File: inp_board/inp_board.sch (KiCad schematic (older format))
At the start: 2 parts

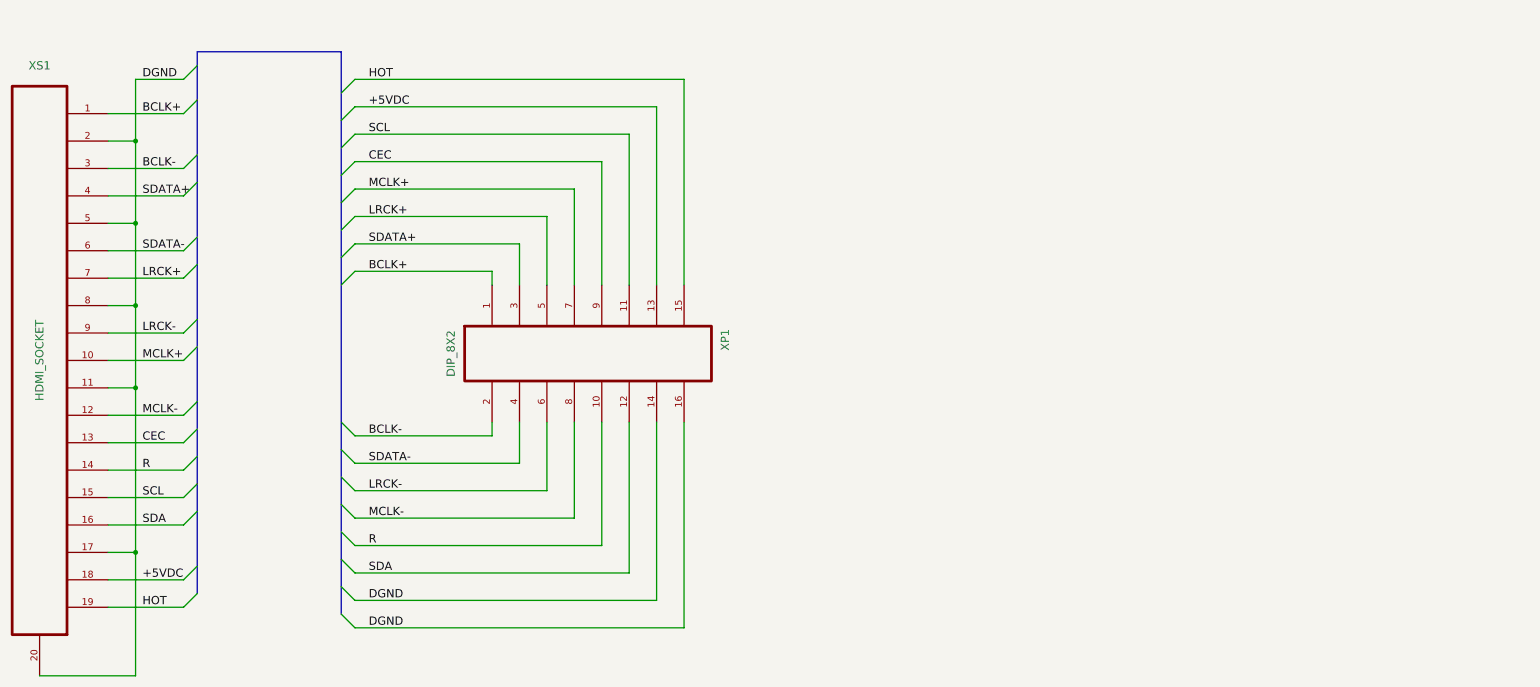
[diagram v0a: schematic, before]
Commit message: spdif part added
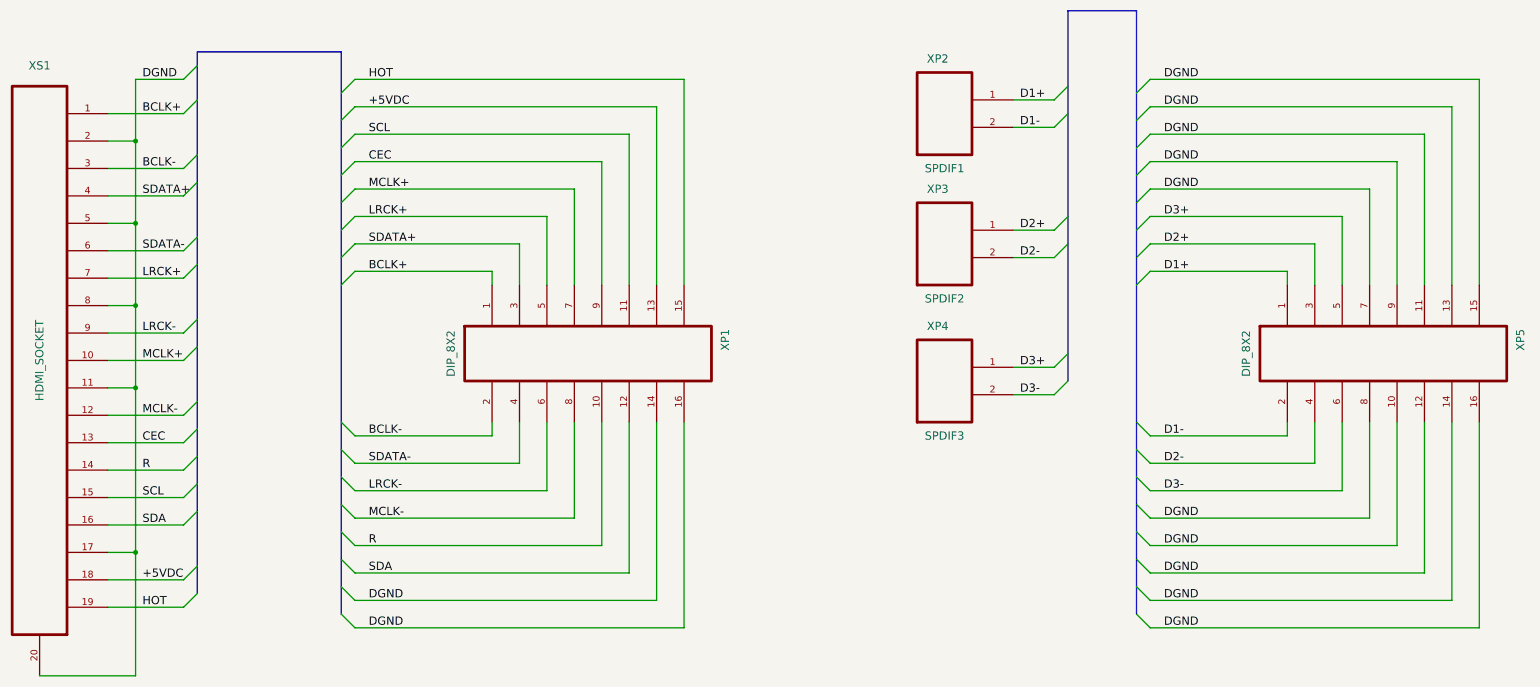
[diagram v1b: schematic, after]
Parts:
- added XP2: SPDIF1, ~, symbol RCA_CONN
- added XP3: SPDIF2, ~, symbol RCA_CONN
- added XP4: SPDIF3, ~, symbol RCA_CONN
- added XP5: DIP_8X2, symbol DIP_8X2
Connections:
- net DGND: now also XP5.10, XP5.11, XP5.12, XP5.13, XP5.14, XP5.15, XP5.16, XP5.7, XP5.8, XP5.9
- new net D1+: XP2.1, XP5.1
- new net D1-: XP2.2, XP5.2
- new net D2+: XP3.1, XP5.3
- new net D2-: XP3.2, XP5.4
- new net D3+: XP4.1, XP5.5
- new net D3-: XP4.2, XP5.6
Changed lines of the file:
@@
 LIBS:valves
 LIBS:gost
-LIBS:InputASRC-cache
+LIBS:inp_board-cache
 EELAYER 27 0
 EELAYER END
-$Descr A4 11693 8268
+$Descr A3 16535 11693
 encoding utf-8
 Sheet 1 1
 Title "noname.sch"
-Date "10 aug 2013"
+Date "12 aug 2013"
 Rev ""
 Comp ""
@@
 Text Label 4800 1600 0    60   ~ 0
 HOT
+$Comp
+L RCA_CONN XP2
+U 1 1 5208E51C
+P 9000 1850
+F 0 "XP2" H 8950 2250 60  0000 C CNN
+F 1 "SPDIF1" H 9000 1450 60  0000 C CNN
+F 2 "~" H 9200 1850 60  0000 C CNN
+F 3 "~" H 9200 1850 60  0000 C CNN
+	1    9000 1850
+	1    0    0    -1
+$EndComp
+$Comp
+L RCA_CONN XP3
+U 1 1 5208E52B
+P 9000 2800
+F 0 "XP3" H 8950 3200 60  0000 C CNN
+F 1 "SPDIF2" H 9000 2400 60  0000 C CNN
+F 2 "~" H 9200 2800 60  0000 C CNN
+F 3 "~" H 9200 2800 60  0000 C CNN
+	1    9000 2800
+	1    0    0    -1
+$EndComp
+$Comp
+L RCA_CONN XP4
+U 1 1 5208E53A
+P 9000 3800
+F 0 "XP4" H 8950 4200 60  0000 C CNN
+F 1 "SPDIF3" H 9000 3400 60  0000 C CNN
+F 2 "~" H 9200 3800 60  0000 C CNN
+F 3 "~" H 9200 3800 60  0000 C CNN
+	1    9000 3800
+	1    0    0    -1
+$EndComp
+Wire Bus Line
+	9900 3800 9900 1100
+Wire Bus Line
+	9900 1100 10400 1100
+Wire Bus Line
+	10400 1100 10400 5500
+Entry Wire Line
+	9800 1750 9900 1650
+Entry Wire Line
+	9800 1950 9900 1850
+Entry Wire Line
+	9800 2700 9900 2600
+Entry Wire Line
+	9800 2900 9900 2800
+Wire Wire Line
+	9500 1750 9800 1750
+Wire Wire Line
+	9800 1950 9500 1950
+Wire Wire Line
+	9500 2700 9800 2700
+Wire Wire Line
+	9500 2900 9800 2900
+Entry Wire Line
+	9800 3700 9900 3600
+Entry Wire Line
+	9800 3900 9900 3800
+Wire Wire Line
+	9500 3700 9800 3700
+Wire Wire Line
+	9500 3900 9800 3900
+Text Label 9550 3900 0    60   ~ 0
+D3-
+Text Label 9550 3700 0    60   ~ 0
+D3+
+Text Label 9550 2900 0    60   ~ 0
+D2-
+Text Label 9550 2700 0    60   ~ 0
+D2+
+Text Label 9550 1950 0    60   ~ 0
+D1-
+Text Label 9550 1750 0    60   ~ 0
+D1+
+Entry Wire Line
+	10400 3100 10500 3000
+Entry Wire Line
+	10400 2900 10500 2800
+Entry Wire Line
+	10400 2700 10500 2600
+Entry Wire Line
+	10400 2500 10500 2400
+Entry Wire Line
+	10400 2300 10500 2200
+Entry Wire Line
+	10400 2100 10500 2000
+Entry Wire Line
+	10400 1900 10500 1800
+Entry Wire Line
+	10400 1700 10500 1600
+Wire Wire Line
+	11500 3100 11500 3000
+Wire Wire Line
+	11500 3000 10500 3000
+Wire Wire Line
+	10500 2800 11700 2800
+Wire Wire Line
+	11700 2800 11700 3100
+Wire Wire Line
+	10500 2600 11900 2600
+Wire Wire Line
+	11900 2600 11900 3100
+Wire Wire Line
+	10500 2400 12100 2400
+Wire Wire Line
+	12100 2400 12100 3100
+Wire Wire Line
+	10500 2200 12300 2200
+Wire Wire Line
+	12300 2200 12300 3100
+Wire Wire Line
+	10500 2000 12500 2000
+Wire Wire Line
+	12500 2000 12500 3100
+Wire Wire Line
+	10500 1800 12700 1800
+Wire Wire Line
+	12700 1800 12700 3100
+Wire Wire Line
+	10500 1600 12900 1600
+Wire Wire Line
+	12900 1600 12900 3100
+Text Label 10600 3000 0    60   ~ 0
+D1+
+Text Label 10600 2800 0    60   ~ 0
+D2+
+Text Label 10600 2600 0    60   ~ 0
+D3+
+Text Label 10600 2400 0    60   ~ 0
+DGND
+Text Label 10600 2200 0    60   ~ 0
+DGND
+Text Label 10600 2000 0    60   ~ 0
+DGND
+$Comp
+L DIP_8X2 XP5
+U 1 1 5208E7E0
+P 12200 3600
+F 0 "XP5" H 12100 4600 60  0000 C CNN
+F 1 "DIP_8X2" H 12200 2600 60  0000 C CNN
+F 2 "" H 12400 3600 60  0000 C CNN
+F 3 "" H 12400 3600 60  0000 C CNN
+	1    12200 3600
+	0    1    1    0
+$EndComp
+Text Label 10600 1800 0    60   ~ 0
+DGND
+Text Label 10600 1600 0    60   ~ 0
+DGND
+Entry Wire Line
+	10400 5500 10500 5600
+Entry Wire Line
+	10400 5300 10500 5400
+Entry Wire Line
+	10400 5100 10500 5200
+Entry Wire Line
+	10400 4900 10500 5000
+Entry Wire Line
+	10400 4700 10500 4800
+Entry Wire Line
+	10400 4500 10500 4600
+Entry Wire Line
+	10400 4300 10500 4400
+Entry Wire Line
+	10400 4100 10500 4200
+Wire Wire Line
+	10500 4200 11500 4200
+Wire Wire Line
+	11500 4200 11500 4100
+Wire Wire Line
+	10500 4400 11700 4400
+Wire Wire Line
+	11700 4400 11700 4100
+Wire Wire Line
+	10500 4600 11900 4600
+Wire Wire Line
+	11900 4600 11900 4100
+Wire Wire Line
+	10500 4800 12100 4800
+Wire Wire Line
+	12100 4800 12100 4100
+Wire Wire Line
+	10500 5000 12300 5000
+Wire Wire Line
+	12300 5000 12300 4100
+Wire Wire Line
+	10500 5200 12500 5200
+Wire Wire Line
+	12500 5200 12500 4100
+Wire Wire Line
+	10500 5400 12700 5400
+Wire Wire Line
+	12700 5400 12700 4100
+Wire Wire Line
+	10500 5600 12900 5600
+Wire Wire Line
+	12900 5600 12900 4100
+Text Label 10600 4200 0    60   ~ 0
+D1-
+Text Label 10600 4400 0    60   ~ 0
+D2-
+Text Label 10600 4600 0    60   ~ 0
+D3-
+Text Label 10600 4800 0    60   ~ 0
+DGND
+Text Label 10600 5000 0    60   ~ 0
+DGND
+Text Label 10600 5200 0    60   ~ 0
+DGND
+Text Label 10600 5400 0    60   ~ 0
+DGND
+Text Label 10600 5600 0    60   ~ 0
+DGND
 $EndSCHEMATC
